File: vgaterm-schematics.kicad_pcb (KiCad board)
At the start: 2 copper layers, 78.7 x 36.3 mm, 23 parts, among them J1 Conn_01x04, J4 Conn_01x15_Socket, J5 Conn_01x15_Socket, J6 Conn_01x10, J7 Conn_01x15, J9 Conn_01x03_Socket, U1 GAL22V10, U2 74AHCT244, U3 IDT7205L12JG, U4 74HCT574

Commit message: updating board based on convos with Seth
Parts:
- added J2: Rst, Connector_PinHeader_2.54mm:PinHeader_1x02_P2.54mm_Vertical, F.Cu at (86.4, 80.0)
- added R2: R, Resistor_SMD:R_0805_2012Metric_Pad1.20x1.40mm_HandSolder, F.Cu at (92.7, 80.5)
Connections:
- J4 pad 4: unconnected-(J4-Pin_4-Pad4) -> /Rst
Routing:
- net /Rst: track 0.00 -> 37.4 mm
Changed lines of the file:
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@@
   (net 16 "unconnected-(J4-Pin_2-Pad2)")
   (net 17 "unconnected-(J4-Pin_3-Pad3)")
-  (net 18 "unconnected-(J4-Pin_4-Pad4)")
+  (net 18 "/Rst")
   (net 19 "unconnected-(J4-Pin_11-Pad11)")
   (net 20 "unconnected-(J4-Pin_12-Pad12)")
@@
     )
   )
+  (footprint "Resistor_SMD:R_0805_2012Metric_Pad1.20x1.40mm_HandSolder" (layer "F.Cu")
+    (at 92.71 80.518)
+    (descr "Resistor SMD 0805 (2012 Metric), square (rectangular) end terminal, IPC_7351 nominal with elongated pad for handsoldering. (Body size source: IPC-SM-782 page 72, https://www.pcb-3d.com/wordpress/wp-content/uploads/ipc-sm-782a_amendment_1_and_2.pdf), generated with kicad-footprint-generator")
+    (tags "resistor handsolder")
+    (property "Sheetfile" "vgaterm-schematics.kicad_sch")
+    (property "Sheetname" "")
+    (property "ki_description" "Resistor")
+    (property "ki_keywords" "R res resistor")
+    (attr smd)
+    (fp_text reference "R2" (at 2.778 0) (layer "F.SilkS")
+        (effects (font (size 1 1) (thickness 0.15)))
+    )
+    (fp_text value "R" (at 0 1.65) (layer "F.Fab")
+        (effects (font (size 1 1) (thickness 0.15)))
+    )
+    (fp_text user "${REFERENCE}" (at 0 0) (layer "F.Fab")
+        (effects (font (size 0.5 0.5) (thickness 0.08)))
+    )
+    (fp_line (start -0.227064 -0.735) (end 0.227064 -0.735)
+      (stroke (width 0.12) (type solid)) (layer "F.SilkS"))
+    (fp_line (start -0.227064 0.735) (end 0.227064 0.735)
+      (stroke (width 0.12) (type solid)) (layer "F.SilkS"))
+    (fp_line (start -1.85 -0.95) (end 1.85 -0.95)
+      (stroke (width 0.05) (type solid)) (layer "F.CrtYd"))
+    (fp_line (start -1.85 0.95) (end -1.85 -0.95)
+      (stroke (width 0.05) (type solid)) (layer "F.CrtYd"))
+    (fp_line (start 1.85 -0.95) (end 1.85 0.95)
+      (stroke (width 0.05) (type solid)) (layer "F.CrtYd"))
+    (fp_line (start 1.85 0.95) (end -1.85 0.95)
+      (stroke (width 0.05) (type solid)) (layer "F.CrtYd"))
+    (fp_line (start -1 -0.625) (end 1 -0.625)
+      (stroke (width 0.1) (type solid)) (layer "F.Fab"))
+    (fp_line (start -1 0.625) (end -1 -0.625)
+      (stroke (width 0.1) (type solid)) (layer "F.Fab"))
+    (fp_line (start 1 -0.625) (end 1 0.625)
+      (stroke (width 0.1) (type solid)) (layer "F.Fab"))
+    (fp_line (start 1 0.625) (end -1 0.625)
+      (stroke (width 0.1) (type solid)) (layer "F.Fab"))
+    (pad "1" smd roundrect (at -1 0) (size 1.2 1.4) (layers "F.Cu" "F.Paste" "F.Mask") (roundrect_rratio 0.208333)
+      (net 18 "/Rst") (pintype "passive"))
+    (pad "2" smd roundrect (at 1 0) (size 1.2 1.4) (layers "F.Cu" "F.Paste" "F.Mask") (roundrect_rratio 0.208333)
+      (net 2 "VCC") (pintype "passive"))
+    (model "${KICAD6_3DMODEL_DIR}/Resistor_SMD.3dshapes/R_0805_2012Metric.wrl"
+      (offset (xyz 0 0 0))
+      (scale (xyz 1 1 1))
+      (rotate (xyz 0 0 0))
+    )
+  )
   (footprint "Connector_PinSocket_2.54mm:PinSocket_1x15_P2.54mm_Vertical" (layer "F.Cu")
     (at 102.955 74.422 -90)
@@
       (net 66 "/U-") (pinfunction "Pin_10") (pintype "passive"))
     (model "${KICAD6_3DMODEL_DIR}/Connector_PinSocket_2.54mm.3dshapes/PinSocket_2x05_P2.54mm_Horizontal.wrl"
+      (offset (xyz 0 0 0))
+      (scale (xyz 1 1 1))
+      (rotate (xyz 0 0 0))
+    )
+  )
+  (footprint "Connector_PinHeader_2.54mm:PinHeader_1x02_P2.54mm_Vertical" (layer "F.Cu")
+    (at 86.36 80.01 90)
+    (descr "Through hole straight pin header, 1x02, 2.54mm pitch, single row")
+    (tags "Through hole pin header THT 1x02 2.54mm single row")
+    (property "Sheetfile" "vgaterm-schematics.kicad_sch")
+    (property "Sheetname" "")
+    (property "ki_description" "Generic connector, single row, 01x02, script generated (kicad-library-utils/schlib/autogen/connector/)")
+    (property "ki_keywords" "connector")
+    (attr through_hole)
+    (fp_text reference "J2" (at 0 -2.33 -270) (layer "B.SilkS")
+        (effects (font (size 1 1) (thickness 0.15)) (justify mirror))
+    )
+    (fp_text value "Rst" (at 1.016 5.334 180) (layer "F.SilkS")
+        (effects (font (size 1 1) (thickness 0.15)))
+    )
+    (fp_text user "${REFERENCE}" (at 0 1.27) (layer "F.Fab")
+        (effects (font (size 1 1) (thickness 0.15)))
+    )
+    (fp_line (start -1.33 -1.33) (end 0 -1.33)
+      (stroke (width 0.12) (type solid)) (layer "F.SilkS"))
+    (fp_line (start -1.33 0) (end -1.33 -1.33)
+      (stroke (width 0.12) (type solid)) (layer "F.SilkS"))
+    (fp_line (start -1.33 1.27) (end -1.33 3.87)
+      (stroke (width 0.12) (type solid)) (layer "F.SilkS"))
+    (fp_line (start -1.33 1.27) (end 1.33 1.27)
+      (stroke (width 0.12) (type solid)) (layer "F.SilkS"))
+    (fp_line (start -1.33 3.87) (end 1.33 3.87)
+      (stroke (width 0.12) (type solid)) (layer "F.SilkS"))
+    (fp_line (start 1.33 1.27) (end 1.33 3.87)
+      (stroke (width 0.12) (type solid)) (layer "F.SilkS"))
+    (fp_line (start -1.8 -1.8) (end -1.8 4.35)
+      (stroke (width 0.05) (type solid)) (layer "F.CrtYd"))
+    (fp_line (start -1.8 4.35) (end 1.8 4.35)
+      (stroke (width 0.05) (type solid)) (layer "F.CrtYd"))
+    (fp_line (start 1.8 -1.8) (end -1.8 -1.8)
+      (stroke (width 0.05) (type solid)) (layer "F.CrtYd"))
+    (fp_line (start 1.8 4.35) (end 1.8 -1.8)
+      (stroke (width 0.05) (type solid)) (layer "F.CrtYd"))
+    (fp_line (start -1.27 -0.635) (end -0.635 -1.27)
+      (stroke (width 0.1) (type solid)) (layer "F.Fab"))
+    (fp_line (start -1.27 3.81) (end -1.27 -0.635)
+      (stroke (width 0.1) (type solid)) (layer "F.Fab"))
+    (fp_line (start -0.635 -1.27) (end 1.27 -1.27)
+      (stroke (width 0.1) (type solid)) (layer "F.Fab"))
+    (fp_line (start 1.27 -1.27) (end 1.27 3.81)
+      (stroke (width 0.1) (type solid)) (layer "F.Fab"))
+    (fp_line (start 1.27 3.81) (end -1.27 3.81)
+      (stroke (width 0.1) (type solid)) (layer "F.Fab"))
+    (pad "1" thru_hole rect (at 0 0 90) (size 1.7 1.7) (drill 1) (layers "*.Cu" "*.Mask")
+      (net 1 "GND") (pinfunction "Pin_1") (pintype "passive"))
+    (pad "2" thru_hole oval (at 0 2.54 90) (size 1.7 1.7) (drill 1) (layers "*.Cu" "*.Mask")
+      (net 18 "/Rst") (pinfunction "Pin_2") (pintype "passive"))
+    (model "${KICAD6_3DMODEL_DIR}/Connector_PinHeader_2.54mm.3dshapes/PinHeader_1x02_P2.54mm_Vertical.wrl"
       (offset (xyz 0 0 0))
       (scale (xyz 1 1 1))
@@
       (net 17 "unconnected-(J4-Pin_3-Pad3)") (pinfunction "Pin_3") (pintype "passive+no_connect"))
     (pad "4" thru_hole oval (at 0 7.62 270) (size 1.7 1.7) (drill 1) (layers "*.Cu" "*.Mask")
-      (net 18 "unconnected-(J4-Pin_4-Pad4)") (pinfunction "Pin_4") (pintype "passive+no_connect"))
+      (net 18 "/Rst") (pinfunction "Pin_4") (pintype "passive"))
     (pad "5" thru_hole oval (at 0 10.16 270) (size 1.7 1.7) (drill 1) (layers "*.Cu" "*.Mask")
       (net 1 "GND") (pinfunction "Pin_5") (pintype "passive"))
@@
     (effects (font (size 1 1) (thickness 0.15)) (justify left bottom))
   )
-  (gr_text "Designed by Seth & Eric\nof Rustbox" (at 84.074 81.28) (layer "F.SilkS")
+  (gr_text "Designed by Seth & Eric\nof Rustbox" (at 84.074 84.074) (layer "F.SilkS")
     (effects (font (size 0.9 0.9) (thickness 0.15)) (justify left bottom))
   )
@@
     (effects (font (size 0.9 0.9) (thickness 0.15)) (justify left bottom))
   )
-  (gr_text "Vgaterm - 2023-10-07" (at 82.042 77.978) (layer "F.SilkS")
+  (gr_text "Vgaterm - 2023-10-07" (at 81.026 77.47) (layer "F.SilkS")
     (effects (font (size 1 1) (thickness 0.15)) (justify left bottom))
   )
@@
   (segment (start 112.363 58.807751) (end 112.363 56.684249) (width 0.25) (layer "F.Cu") (net 15))
   (segment (start 70.697 67.818) (end 75.465 63.05) (width 0.25) (layer "F.Cu") (net 15))
+  (segment (start 90.17 80.01) (end 90.678 80.518) (width 0.25) (layer "F.Cu") (net 18))
+  (segment (start 90.678 80.518) (end 91.71 80.518) (width 0.25) (layer "F.Cu") (net 18))
+  (segment (start 88.9 80.01) (end 90.17 80.01) (width 0.25) (layer "F.Cu") (net 18))
+  (segment (start 93.98 55.626) (end 95.335 54.271) (width 0.25) (layer "B.Cu") (net 18))
+  (segment (start 88.9 80.01) (end 88.9 69.824878) (width 0.25) (layer "B.Cu") (net 18))
+  (segment (start 88.9 69.824878) (end 87.352 68.276878) (width 0.25) (layer "B.Cu") (net 18))
+  (segment (start 95.335 54.271) (end 95.335 51.562) (width 0.25) (layer "B.Cu") (net 18))
+  (segment (start 87.352 58.952) (end 90.678 55.626) (width 0.25) (layer "B.Cu") (net 18))
+  (segment (start 90.678 55.626) (end 93.98 55.626) (width 0.25) (layer "B.Cu") (net 18))
+  (segment (start 87.352 68.276878) (end 87.352 58.952) (width 0.25) (layer "B.Cu") (net 18))
   (segment (start 137.16 52.832) (end 135.382 54.61) (width 0.25) (layer "F.Cu") (net 21))
   (segment (start 135.382 63.264) (end 132.86 65.786) (width 0.25) (layer "F.Cu") (net 21))

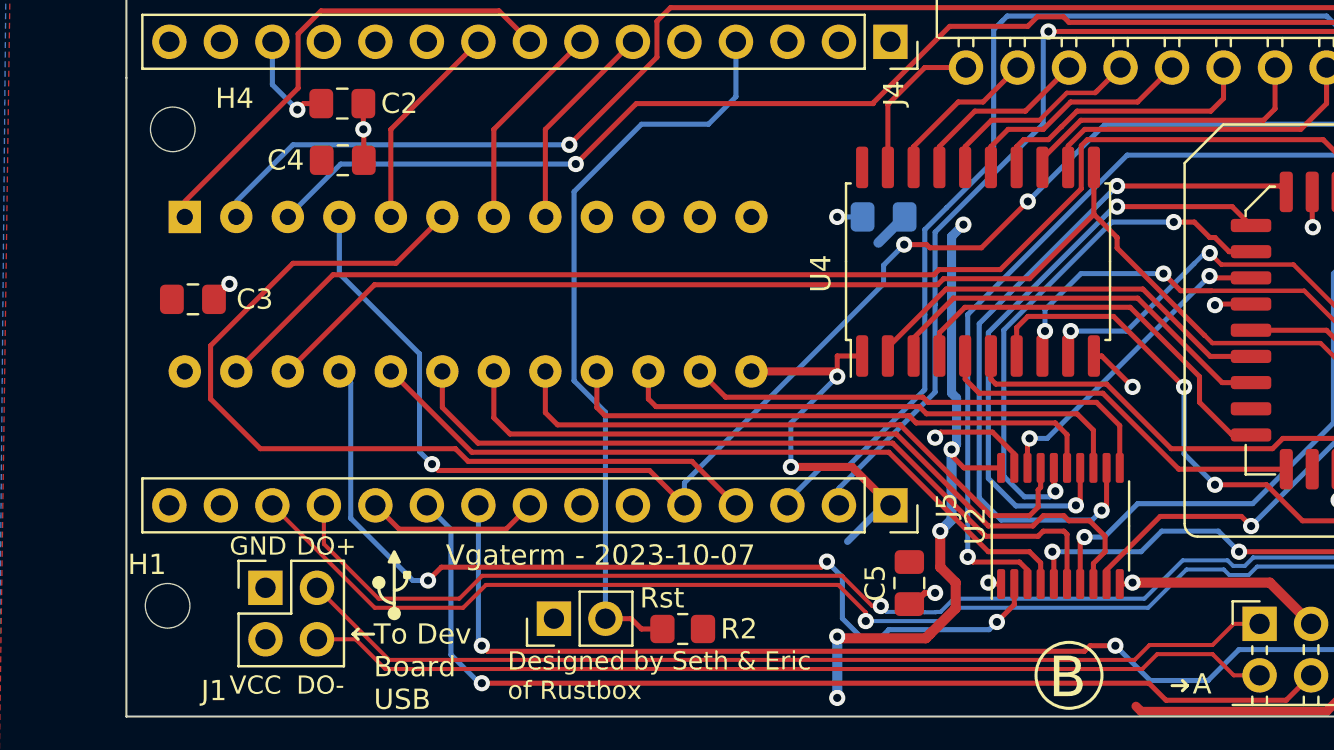
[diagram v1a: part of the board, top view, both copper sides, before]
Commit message: updating timing board hsync vsync delay
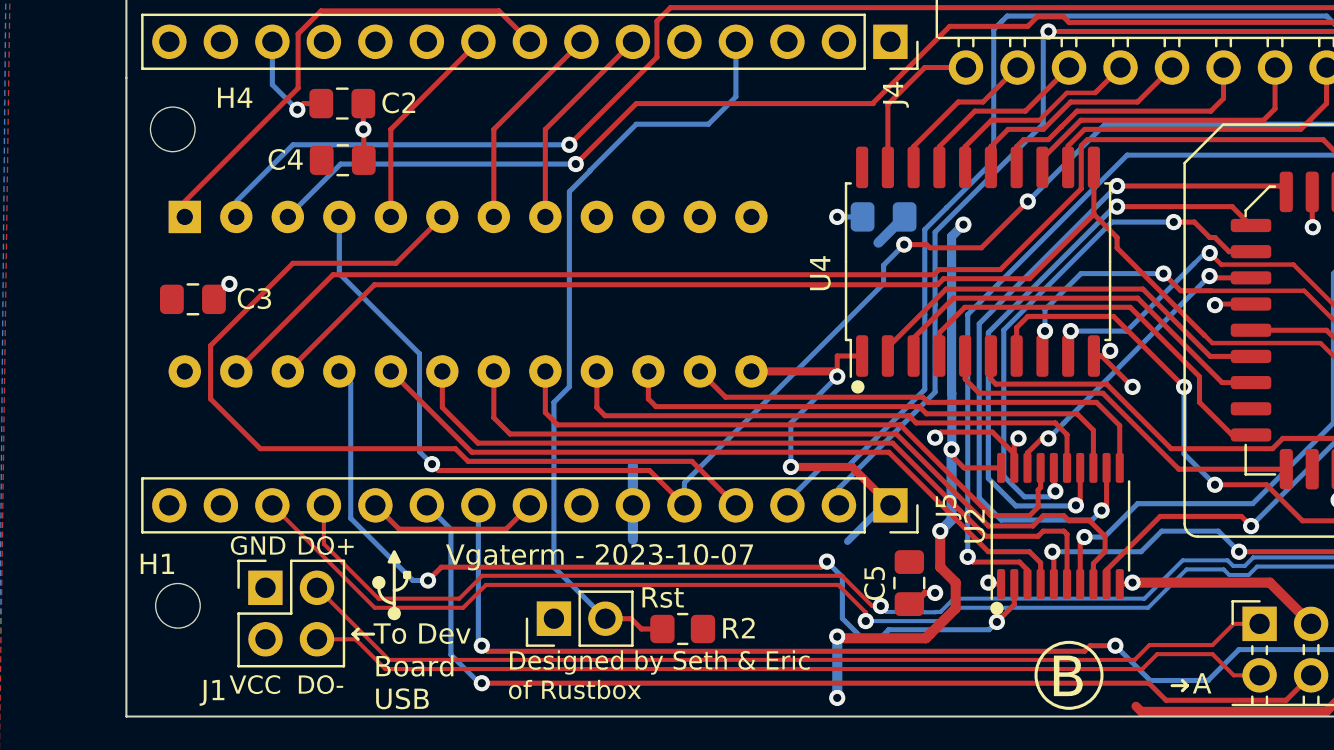
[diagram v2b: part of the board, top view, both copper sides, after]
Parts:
- moved H1 0.51 mm to (67.8, 79.4)
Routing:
- net GND: track 68.0 -> 73.7 mm, vias 15 -> 17
- net /Rst: track 37.4 -> 38.3 mm
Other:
- board text added: "DO- U0Txd VCC VCC U- DO+ GND U0Rxd GND U+"
- board text added: "P0 P1 P2 P3 P4 P5 P6 P7 KbRx KbTx Clk Vis ~{Start} GND Vcc"

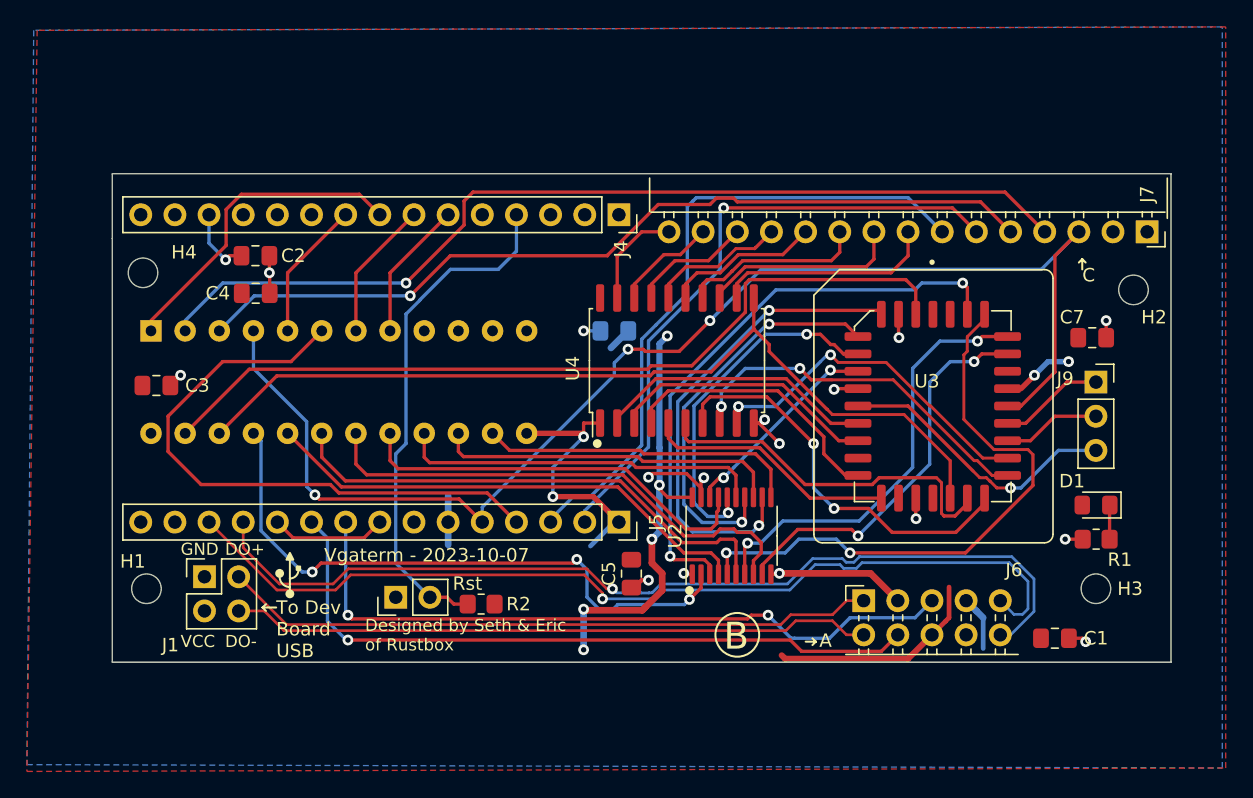
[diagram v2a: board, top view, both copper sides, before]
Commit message: board updates and adding vga breakout
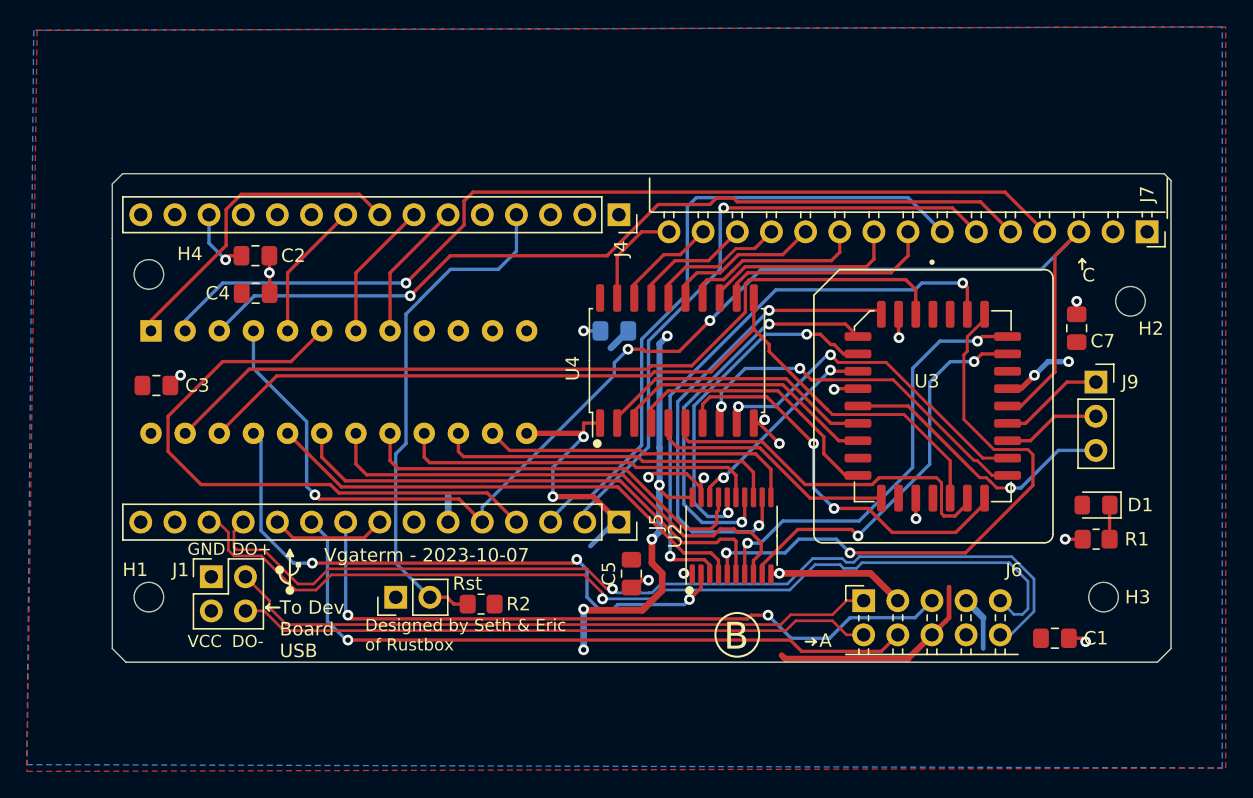
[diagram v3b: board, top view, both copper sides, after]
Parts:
- moved C7 1.35 mm to (137.0, 60.0), turned to -90 degrees
- moved H2 0.88 mm to (141.0, 58.0)
- moved H3 0.85 mm to (139.0, 80.0)
- moved H1 0.65 mm to (68.0, 80.0)
- moved J1 0.51 mm to (72.6, 78.5)
- moved H4 0.45 mm to (68.0, 56.0)
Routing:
- net GND: track 73.7 -> 71.7 mm
- net /U-: track 70.7 -> 71.7 mm
- net /U+: track 71.1 -> 71.8 mm
- net /D1: track 37.7 -> 37.0 mm
- net /D0: track 46.4 -> 45.8 mm
- net /DO-: track 47.8 -> 47.3 mm
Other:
- outline, holes or cut-outs redrawn

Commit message: current boards
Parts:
- added C6: 220n, Capacitor_SMD:C_0805_2012Metric_Pad1.18x1.45mm_HandSolder, F.Cu at (81.6, 64.8)
- added R3: 330, Resistor_SMD:R_0805_2012Metric_Pad1.20x1.40mm_HandSolder, F.Cu at (77.2, 64.8)
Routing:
- net GND: track 71.7 -> 77.6 mm, vias 17 -> 18
- net Net-(C6-Pad1): track 0.00 -> 2.30 mm
